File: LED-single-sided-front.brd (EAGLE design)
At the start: 48.3 x 48.3 mm, 21 parts, among them Q1 BUK98180-100A, Q2 BUK98180-100A, Q3 BUK98180-100A, Q4 BUK98180-100A

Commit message: mk9 brah.
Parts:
- R1, R2, R3, R4, R5, R6: device rcl:0204/7 -> rcl:R1206
- moved LOGO1 15.7 mm to (19.4, 9.21)
- moved R2 1.42 mm to (30.5, 20.0)
- moved R3 0.71 mm to (32.7, 18.7)
- moved R5 0.64 mm to (24.1, 32.4)
- moved R4 0.32 mm to (24.1, 34.6)
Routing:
- net WHITE: track 17.7 -> 22.8 mm
- net N$2: track 11.4 -> 14.6 mm
- net N$31: track 11.7 -> 14.9 mm
- net N$32: track 13.9 -> 17.0 mm
- net N$34: track 11.5 -> 14.4 mm
- net N$5: track 11.7 -> 14.6 mm
- net N$6: track 13.9 -> 16.8 mm
- net N$30: track 12.8 -> 15.2 mm
- net N$4: track 12.8 -> 15.2 mm
- net N$35: track 14.9 -> 17.3 mm
- net N$33: track 13.0 -> 15.3 mm
- net N$3: track 14.3 -> 16.4 mm
- net N$1: track 12.9 -> 14.8 mm
- net P_WHITE: track 36.6 -> 38.4 mm
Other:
- board text added: "@matthewbaggett"
- board text added: "WifiLight mk9"
- board text added: "git.io/vwt9H"

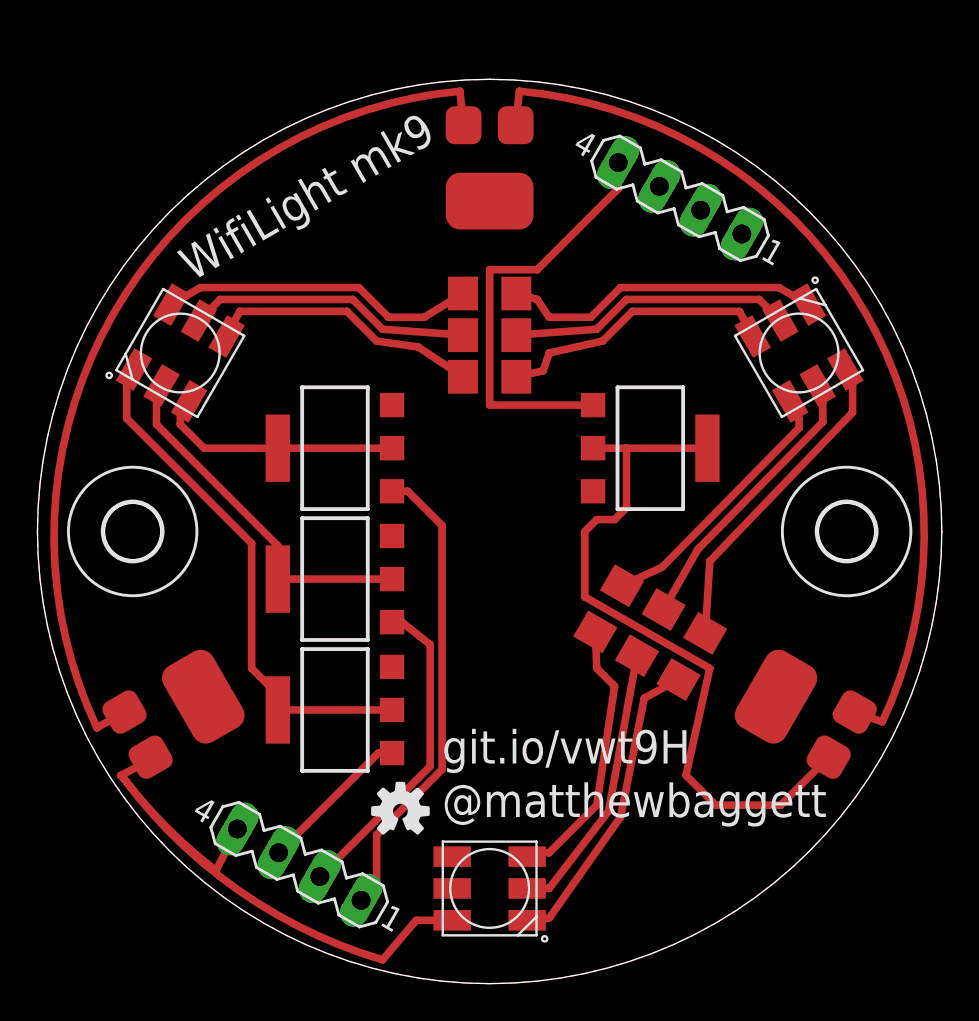
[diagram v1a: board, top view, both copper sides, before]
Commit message: Put hole in middle of board (hurr durr donuts). Change to smaller mosfets. Add pulldown resistors.
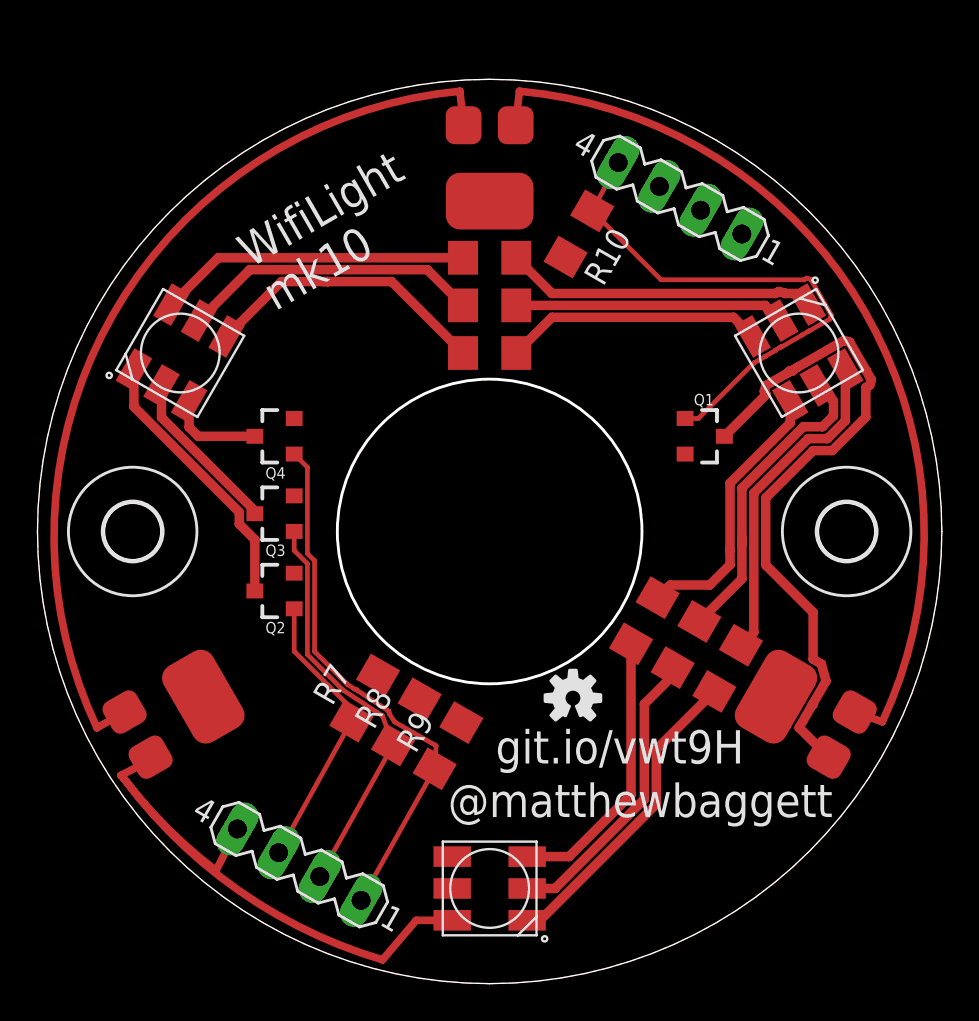
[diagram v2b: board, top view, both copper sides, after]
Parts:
- added R10, R7, R8, R9: 10k, rcl:R1206
- Q1, Q2, Q3, Q4: value BUK98180-100A -> 5.8A/30V/35mΩ; device nxp_60:SOT223 -> SparkFun-DiscreteSemi:SOT23-3
- R1, R2, R3, R4: value 0 -> 50Ω
- moved LOGO1 11.0 mm to (28.6, 15.2)
- moved Q2 7.10 mm to (12.7, 21.0)
- moved Q3 4.72 mm to (12.7, 25.1)
- moved Q4 3.24 mm to (12.7, 29.2)
- moved Q1 2.93 mm to (35.6, 29.2)
- moved R3 2.01 mm to (34.6, 18.1)
- moved R1 2.01 mm to (36.8, 16.8)
- moved R2 2.01 mm to (32.4, 19.4)
- moved R6 1.91 mm to (24.1, 38.7)
- moved R4 1.59 mm to (24.1, 36.2)
- moved R5 1.27 mm to (24.1, 33.7)
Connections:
- net BLUE: now also R7.1
- net GND: now also Q1.2, Q2.2, Q3.2, Q4.2, R10.2, R7.2, R8.2, R9.2; no longer Q1.3, Q2.3, Q3.3, Q4.3
- net GREEN: now also R9.1
- net P_BLUE: now also Q2.3; no longer Q2.2, Q2.4
- net P_GREEN: now also Q4.3; no longer Q4.2, Q4.4
- net P_RED: now also Q3.3; no longer Q3.2, Q3.4
- net P_WHITE: now also Q1.3; no longer Q1.2, Q1.4
- net RED: now also R8.1
- net WHITE: now also R10.1
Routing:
- net P_BLUE: track 27.8 -> 14.5 mm
- net P_RED: track 19.2 -> 8.90 mm
- net P_GREEN: track 13.3 -> 5.09 mm
- net BLUE: track 8.26 -> 15.3 mm
- net WHITE: track 22.8 -> 28.2 mm
- net RED: track 17.3 -> 21.7 mm
- net GREEN: track 25.2 -> 28.6 mm
- net P_WHITE: track 38.4 -> 36.6 mm
- net N$33: track 15.3 -> 16.9 mm
- net N$5: track 14.6 -> 15.7 mm
- net N$1: track 14.8 -> 15.9 mm
- net N$31: track 14.9 -> 13.8 mm
- net N$30: track 15.2 -> 14.4 mm
- net N$4: track 15.2 -> 16.0 mm
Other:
- outline, holes or cut-outs redrawn
- board text added: "WifiLight mk10"
- board text removed: "WifiLight mk9"
